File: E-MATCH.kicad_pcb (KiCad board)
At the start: 4 copper layers, 22 parts, among them IC1 NCV81071BZR2G, IC2 NCV81071BZR2G, J1 691210910002, J2 691210910002, J3 691210910002, J4 691210910002, J5 DC Jack, Q1 AOSP36326C, Q2 AOSP36326C, Q3 AOSP36326C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

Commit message: Schematic Cleanup
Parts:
- removed LED1: LTST-C170GKT, Smd_Led:LED_LTST-C170GKT_LTO
- added LED2: LTST-C170GKT, Smd_Led:LED_LTST-C170GKT_LTO, F.Cu at (170.2, 99.0)
- U1: footprint Current Sensor:D0008A-MFG -> Current Sensor:D0008A-IPC_A

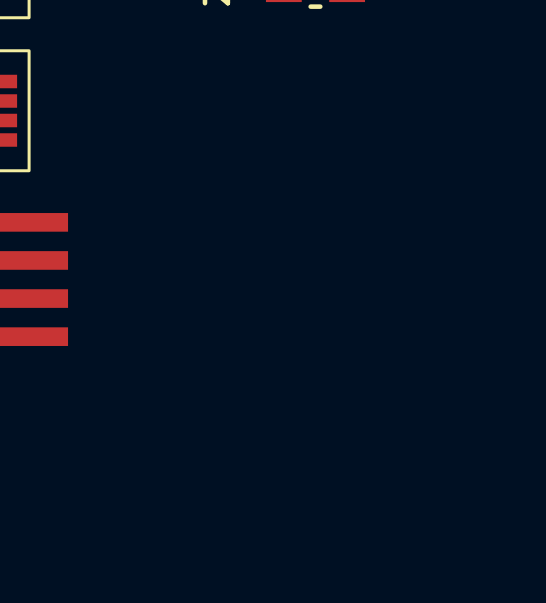
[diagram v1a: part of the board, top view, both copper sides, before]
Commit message: SMD_Resistor added
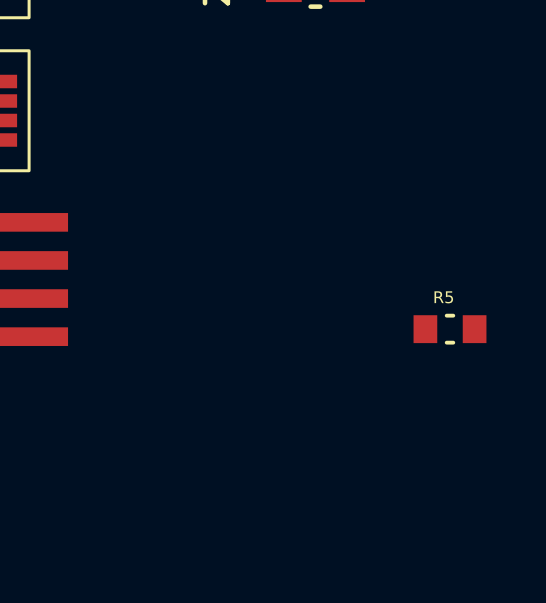
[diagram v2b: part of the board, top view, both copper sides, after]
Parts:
- added R5: 330R, SMD_RESISTOR:RESC1608X55N, F.Cu at (174.7, 110.5)

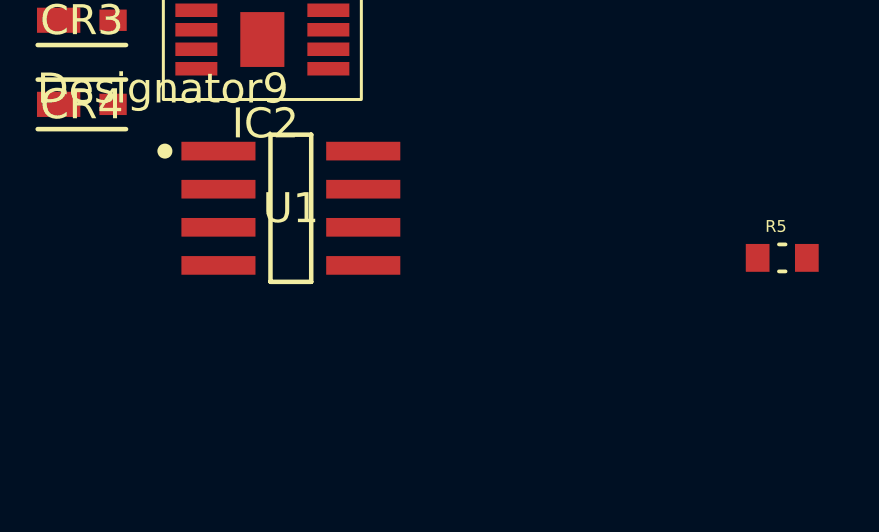
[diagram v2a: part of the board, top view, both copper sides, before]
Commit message: 3d model reassociation
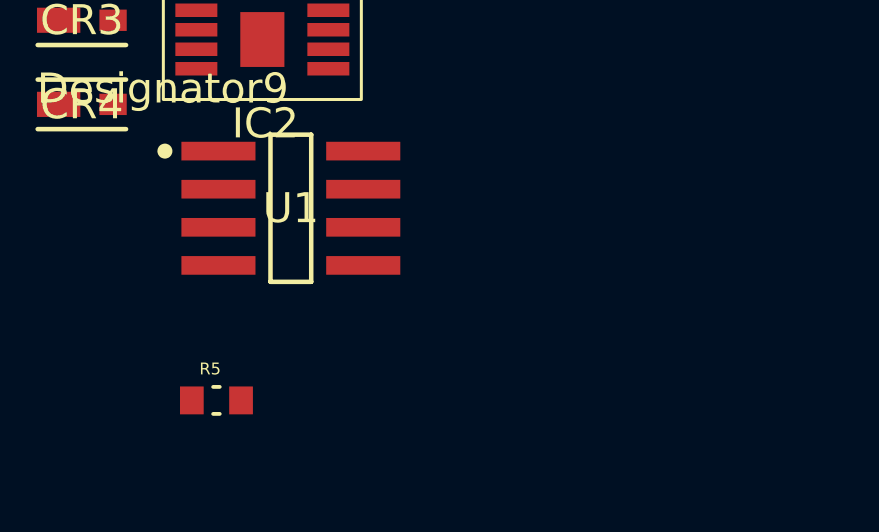
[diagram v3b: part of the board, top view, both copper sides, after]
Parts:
- moved R5 19.4 mm to (155.8, 115.2)
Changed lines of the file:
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@@
 	(footprint "SMD_RESISTOR:RESC1608X55N"
 		(layer "F.Cu")
-		(at 174.68 110.5)
+		(at 155.82 115.25)
 		(property "Reference" "R5"
 			(at -0.21 -1.05 0)
@@
 		(model "${KIPRJMOD}/Custom E-CAD Models/SMD-Resistor/RC0603JR-07330RL/RC0603JR-07330RL.step"
 			(offset
-				(xyz 0 0 0)
+				(xyz 0 -0 0)
 			)
 			(scale
@@
 			)
 			(rotate
-				(xyz 0 0 0)
+				(xyz -90 -0 -0)
 			)
 		)
@@
 		)
 		(embedded_fonts no)
+		(model "${KIPRJMOD}/Custom E-CAD Models/3D Models/Current Sensor/D0008A.stp"
+			(offset
+				(xyz 0 0 0)
+			)
+			(scale
+				(xyz 1 1 1)
+			)
+			(rotate
+				(xyz 0 0 0)
+			)
+		)
 	)
 	(footprint "Screw_Terminal:691210910002"

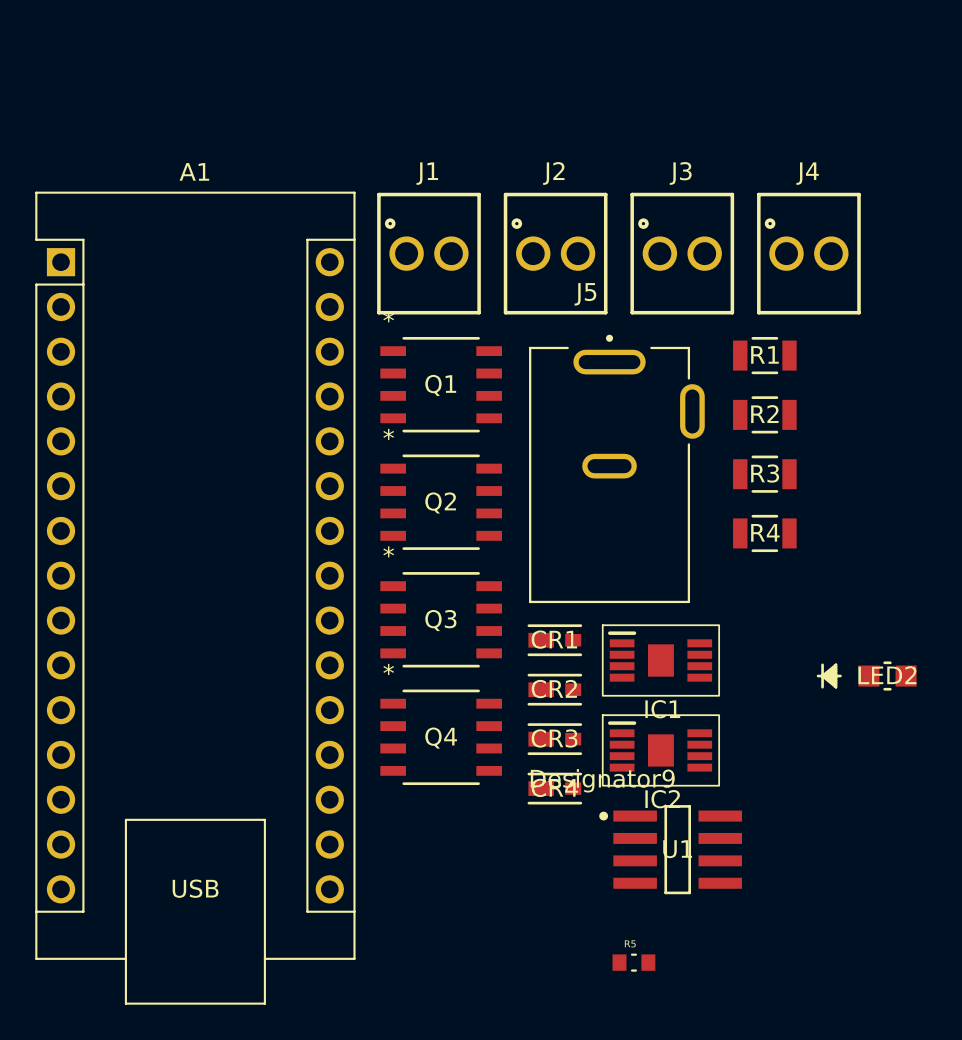
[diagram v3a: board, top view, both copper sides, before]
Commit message: modified some footprints
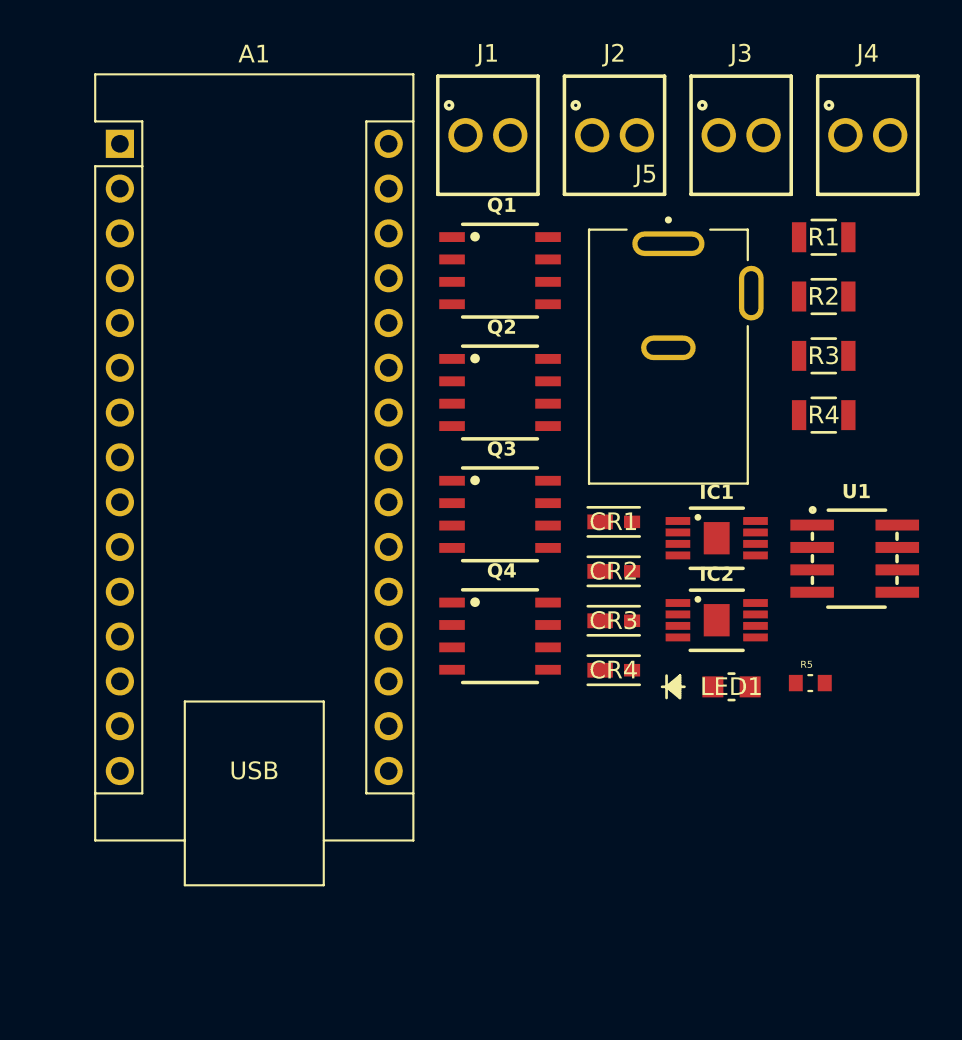
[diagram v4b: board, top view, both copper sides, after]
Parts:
- removed LED2: LTST-C170GKT, Smd_Led:LED_LTST-C170GKT_LTO
- added LED1: LTST-C170GKT, Smd_Led:LED_LTST-C170GKT_LTO, F.Cu at (161.4, 99.6)
- moved U1 19.3 mm to (168.3, 92.3)
- moved R5 18.7 mm to (165.8, 99.4)
- moved IC2 8.03 mm to (160.5, 95.8)
- moved IC1 7.62 mm to (160.5, 91.2)
- moved J1 7.49 mm to (147.5, 68.3)
- moved R1 7.49 mm to (166.6, 74.1)
- moved R4 7.49 mm to (166.6, 84.2)
- moved A1 7.49 mm to (126.7, 68.8)
- moved CR1 7.49 mm to (154.7, 90.3)
- moved CR3 7.49 mm to (154.7, 95.9)
- moved CR4 7.49 mm to (154.7, 98.7)
- moved J2 7.49 mm to (154.7, 68.3)
- moved J3 7.49 mm to (161.9, 68.3)
- moved J4 7.49 mm to (169.1, 68.3)
- moved R2 7.49 mm to (166.6, 77.5)
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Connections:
- R5 pad 1: unconnected-(R5-Pad1) -> 5V
- R5 pad 2: unconnected-(R5-Pad2) -> Net-(LED1-Pad2)

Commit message: Cleaned a few footprints
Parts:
- moved CR4 2.08 mm to (154.7, 100.8)
- moved CR3 1.63 mm to (154.7, 97.5)
- moved CR2 1.19 mm to (154.7, 94.2)
- moved R4 0.79 mm to (166.6, 85.0)
- moved CR1 0.75 mm to (154.7, 91.0)
- moved R3 0.40 mm to (166.6, 81.2)
- moved R1 0.37 mm to (166.6, 73.8)
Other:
- board outline added: 63.8 x 63 mm
- board text added: "E-MATCH FIRING CIRCUIT"
- board text added: "UMSATS ROCKETRY"

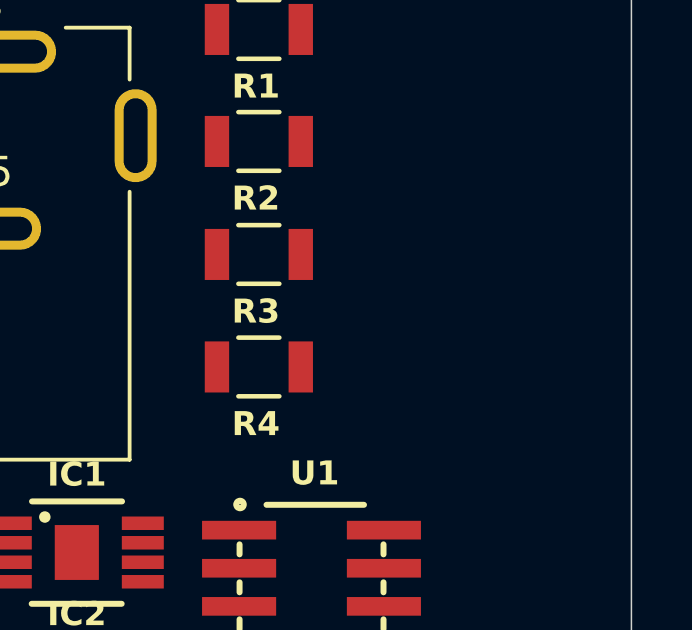
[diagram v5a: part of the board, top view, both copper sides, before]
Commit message: added a decoupling capacitor
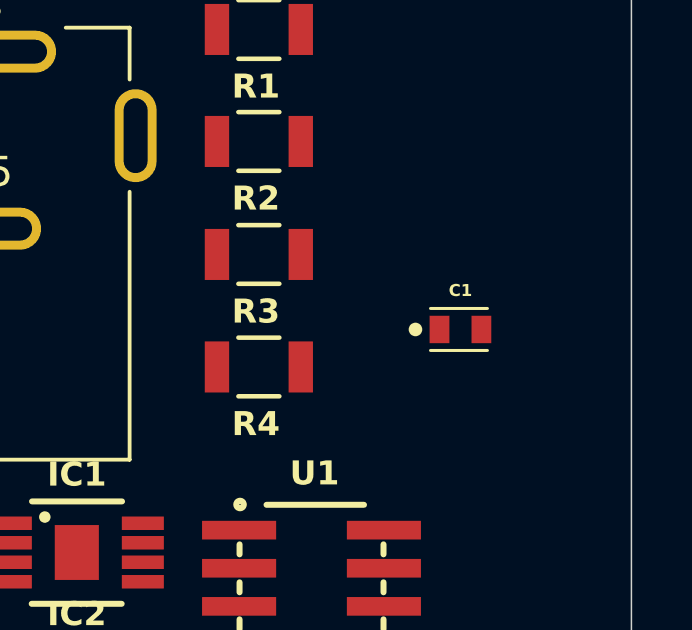
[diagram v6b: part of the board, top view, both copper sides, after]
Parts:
- added C1: 0.1u, 0.1 uF Cap:CAP_C0603C104K5RAC3121_KEM-L, F.Cu at (173.3, 83.8)

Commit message: made minor adjustments in both schematic and pcb layout
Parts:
- removed C1: 0.1u, 0.1 uF Cap:CAP_C0603C104K5RAC3121_KEM-L
- added C4: C_Small, Capacitor_SMD:C_0603_1608Metric, F.Cu at (174.2, 80.0)
- added C5: C_Small, Capacitor_SMD:C_0603_1608Metric, F.Cu at (174.2, 82.5)
- added C6: C_Small, Capacitor_SMD:C_0603_1608Metric, F.Cu at (174.2, 85.0)
- moved LED1 1.40 mm to (161.2, 101.0)

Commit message: some changes
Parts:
- added M1: FDC8878, FDC8878:SuperSot6_SOT-23-6_1P6X2P9_ONS, F.Cu at (145.5, 107.5)
- added Q5: FDD1600N10ALZ, FDD1600N10ALZ:TO252_FDD1600_ONS-L, F.Cu at (155.4, 99.4)
- added REF**: MountingHole_2.7mm_Pad_Via, MountingHole:MountingHole_2.7mm_Pad_Via, F.Cu at (106.5, 141.5)
- added REF**: MountingHole_2.7mm_Pad_Via, MountingHole:MountingHole_2.7mm_Pad_Via, F.Cu at (106.5, 51.5)
- added REF**: MountingHole_2.7mm_Pad_Via, MountingHole:MountingHole_2.7mm_Pad_Via, F.Cu at (196.5, 141.5)
- added REF**: MountingHole_2.7mm_Pad_Via, MountingHole:MountingHole_2.7mm_Pad_Via, F.Cu at (196.5, 51.5)
- moved C4 34.5 mm to (153.4, 107.5)
- moved C5 34.5 mm to (153.4, 110.0)
- moved C6 34.5 mm to (153.4, 112.5)
- moved R5 24.0 mm to (144.8, 111.0)
- moved U1 17.0 mm to (163.6, 108.7)
- moved LED1 14.3 mm to (163.9, 115.0)
- moved IC1 8.71 mm to (167.5, 96.4)
- moved IC2 8.71 mm to (167.5, 101.0)
- moved CR1 8.25 mm to (161.7, 95.4)
- moved CR2 8.03 mm to (161.7, 98.2)
- moved CR3 7.81 mm to (161.7, 101.0)
- moved CR4 7.62 mm to (161.7, 103.9)
- moved R1 5.67 mm to (165.4, 79.3)
- moved A1 5.30 mm to (125.5, 74.0)
- moved J1 5.30 mm to (146.4, 73.5)
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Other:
- board size 63.8 x 63 mm -> 100 x 100 mm
- board text removed: "E-MATCH FIRING CIRCUIT"
- board text removed: "UMSATS ROCKETRY"
